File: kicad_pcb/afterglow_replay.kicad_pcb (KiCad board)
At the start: 2 copper layers, 49 x 111 mm, 106 parts, among them Q1 BC807, Q2 BC807, Q3 BC807, Q4 BC807, Q5 BC807, Q6 BC807, Q7 BC807, Q8 BC807, U1 ATmega328P-AU, U2 TLC5916IN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

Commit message: PCB v1.1
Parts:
- added USB PWR: USB_B_Micro, Connectors_USB:USB_Micro-B_Molex-105017-0001, B.Cu at (133.4, 46.4)
- C2: value 100nF -> 10uF; footprint Capacitors_SMD:C_0805_HandSoldering -> Capacitors_THT:CP_Radial_D5.0mm_P2.00mm
- C3, C4: value 16pF -> 18pF
- moved C2 65.0 mm to (128.3, 76.1)
- moved G*** 1.00 mm to (121.2, 53.5)
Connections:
- C2 pad 1: /RESET -> GND
- C2 pad 2: Net-(C2-Pad2) -> +3V3
- D12 pad 2: Net-(D12-Pad2) -> Net-(D11-Pad2)
- D13 pad 2: Net-(D12-Pad2) -> Net-(D11-Pad2)
- D14 pad 2: Net-(D12-Pad2) -> Net-(D11-Pad2)
- D15 pad 2: Net-(D12-Pad2) -> Net-(D11-Pad2)
- D16 pad 2: Net-(D12-Pad2) -> Net-(D11-Pad2)
- D17 pad 2: Net-(D12-Pad2) -> Net-(D11-Pad2)
- D18 pad 2: Net-(D12-Pad2) -> Net-(D11-Pad2)
- D22 pad 2: Net-(D22-Pad2) -> Net-(D21-Pad2)
- D23 pad 2: Net-(D22-Pad2) -> Net-(D21-Pad2)
- D24 pad 2: Net-(D22-Pad2) -> Net-(D21-Pad2)
- D25 pad 2: Net-(D22-Pad2) -> Net-(D21-Pad2)
- D26 pad 2: Net-(D22-Pad2) -> Net-(D21-Pad2)
- D27 pad 2: Net-(D22-Pad2) -> Net-(D21-Pad2)
- D28 pad 2: Net-(D22-Pad2) -> Net-(D21-Pad2)
- D32 pad 2: Net-(D32-Pad2) -> Net-(D31-Pad2)
- D33 pad 2: Net-(D32-Pad2) -> Net-(D31-Pad2)
- D34 pad 2: Net-(D32-Pad2) -> Net-(D31-Pad2)
- D35 pad 2: Net-(D32-Pad2) -> Net-(D31-Pad2)
- D36 pad 2: Net-(D32-Pad2) -> Net-(D31-Pad2)
- D37 pad 2: Net-(D32-Pad2) -> Net-(D31-Pad2)
- D38 pad 2: Net-(D32-Pad2) -> Net-(D31-Pad2)
- D42 pad 2: Net-(D42-Pad2) -> Net-(D41-Pad2)
- D43 pad 2: Net-(D42-Pad2) -> Net-(D41-Pad2)
- D44 pad 2: Net-(D42-Pad2) -> Net-(D41-Pad2)
- D45 pad 2: Net-(D42-Pad2) -> Net-(D41-Pad2)
- D46 pad 2: Net-(D42-Pad2) -> Net-(D41-Pad2)
- D47 pad 2: Net-(D42-Pad2) -> Net-(D41-Pad2)
- D48 pad 2: Net-(D42-Pad2) -> Net-(D41-Pad2)
- D52 pad 2: Net-(D52-Pad2) -> Net-(D51-Pad2)
- D53 pad 2: Net-(D52-Pad2) -> Net-(D51-Pad2)
- D54 pad 2: Net-(D52-Pad2) -> Net-(D51-Pad2)
- D55 pad 2: Net-(D52-Pad2) -> Net-(D51-Pad2)
- D56 pad 2: Net-(D52-Pad2) -> Net-(D51-Pad2)
- D57 pad 2: Net-(D52-Pad2) -> Net-(D51-Pad2)
- D58 pad 2: Net-(D52-Pad2) -> Net-(D51-Pad2)
- D62 pad 2: Net-(D62-Pad2) -> Net-(D61-Pad2)
- D63 pad 2: Net-(D62-Pad2) -> Net-(D61-Pad2)
- D64 pad 2: Net-(D62-Pad2) -> Net-(D61-Pad2)
- D65 pad 2: Net-(D62-Pad2) -> Net-(D61-Pad2)
- D66 pad 2: Net-(D62-Pad2) -> Net-(D61-Pad2)
- D67 pad 2: Net-(D62-Pad2) -> Net-(D61-Pad2)
- D68 pad 2: Net-(D62-Pad2) -> Net-(D61-Pad2)
- D72 pad 2: Net-(D72-Pad2) -> Net-(D71-Pad2)
- D73 pad 2: Net-(D72-Pad2) -> Net-(D71-Pad2)
- D74 pad 2: Net-(D72-Pad2) -> Net-(D71-Pad2)
- D75 pad 2: Net-(D72-Pad2) -> Net-(D71-Pad2)
- D76 pad 2: Net-(D72-Pad2) -> Net-(D71-Pad2)
- D77 pad 2: Net-(D72-Pad2) -> Net-(D71-Pad2)
- D78 pad 2: Net-(D72-Pad2) -> Net-(D71-Pad2)
- D82 pad 2: Net-(D82-Pad2) -> Net-(D81-Pad2)
- D83 pad 2: Net-(D82-Pad2) -> Net-(D81-Pad2)
- D84 pad 2: Net-(D82-Pad2) -> Net-(D81-Pad2)
- D85 pad 2: Net-(D82-Pad2) -> Net-(D81-Pad2)
- D86 pad 2: Net-(D82-Pad2) -> Net-(D81-Pad2)
- D87 pad 2: Net-(D82-Pad2) -> Net-(D81-Pad2)
- D88 pad 2: Net-(D82-Pad2) -> Net-(D81-Pad2)
- ISP pad 5: Net-(C2-Pad2) -> /RESET
- R12 pad 1: /SCK -> Net-(R12-Pad1)
- U1 pad 13: /SCK -> Net-(R12-Pad1)
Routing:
- net Net-(D81-Pad2): track 30.0 -> 161.5 mm, vias 1 -> 4
- net Net-(D82-Pad2): track 130.4 -> 0.00 mm, vias 3 -> 0
- net Net-(D21-Pad2): track 58.0 -> 149.7 mm
- net Net-(D22-Pad2): track 91.2 -> 0.00 mm
- net Net-(D31-Pad2): track 45.2 -> 119.6 mm, vias 1 -> 4
- net Net-(D32-Pad2): track 72.5 -> 0.00 mm, vias 2 -> 0
- net Net-(D51-Pad2): track 22.2 -> 90.0 mm, vias 1 -> 3
- net Net-(D52-Pad2): track 66.5 -> 0.00 mm, vias 2 -> 0
- net Net-(R12-Pad1): track 0.00 -> 52.4 mm, vias 0 -> 4
- net Net-(D61-Pad2): track 15.7 -> 63.7 mm
- net Net-(D62-Pad2): track 41.2 -> 0.00 mm
- net Net-(D71-Pad2): track 57.8 -> 97.7 mm
- net Net-(D72-Pad2): track 37.4 -> 0.00 mm
- net Net-(D11-Pad2): track 30.9 -> 64.1 mm, vias 1 -> 2
- net Net-(D41-Pad2): track 40.9 -> 70.8 mm
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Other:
- board text added: "REPLAY v1.1"
- board text removed: "REPLAY v1.0"

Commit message: PCB v1.2
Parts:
- added J5: Conn_01x02_Male, Pin_Headers:Pin_Header_Straight_1x02_Pitch2.54mm, B.Cu at (123.1, 45.9)
- added J6: Conn_01x02_Male, Pin_Headers:Pin_Header_Straight_1x02_Pitch2.54mm, B.Cu at (143.0, 45.9)
- C2: footprint Capacitors_THT:CP_Radial_D5.0mm_P2.00mm -> Capacitors_SMD:CP_Elec_4x5.3
- J4: renamed from USB PWR
- moved C2 1.03 mm to (127.4, 75.6)
- renumbered PWR to J1, SER to J2, ISP to J3, RST to SW1
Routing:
- net +3V3: track 361.8 -> 391.3 mm
- net GND: track 235.1 -> 247.5 mm
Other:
- board text added: "REPLAY v1.2"
- board text removed: "REPLAY v1.1"

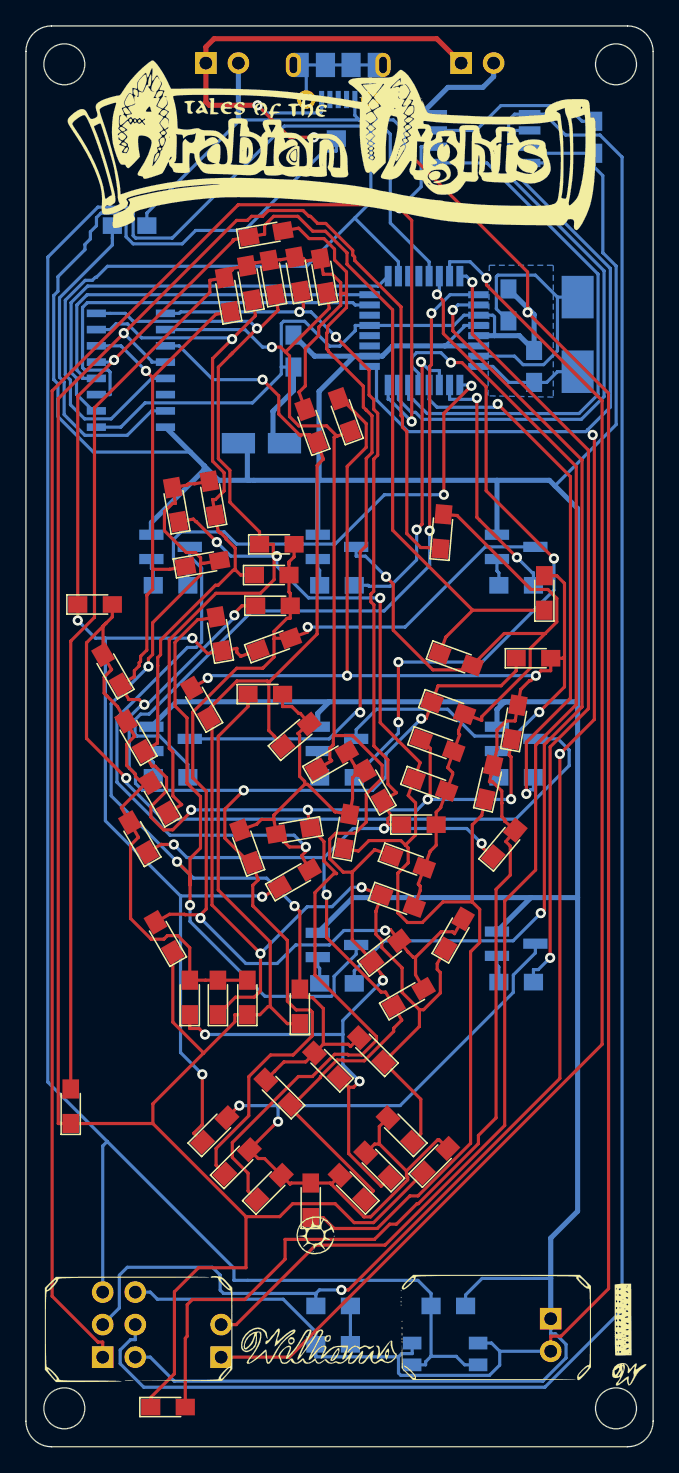
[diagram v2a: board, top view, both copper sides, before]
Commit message: PCB v1.2 slightly less wide
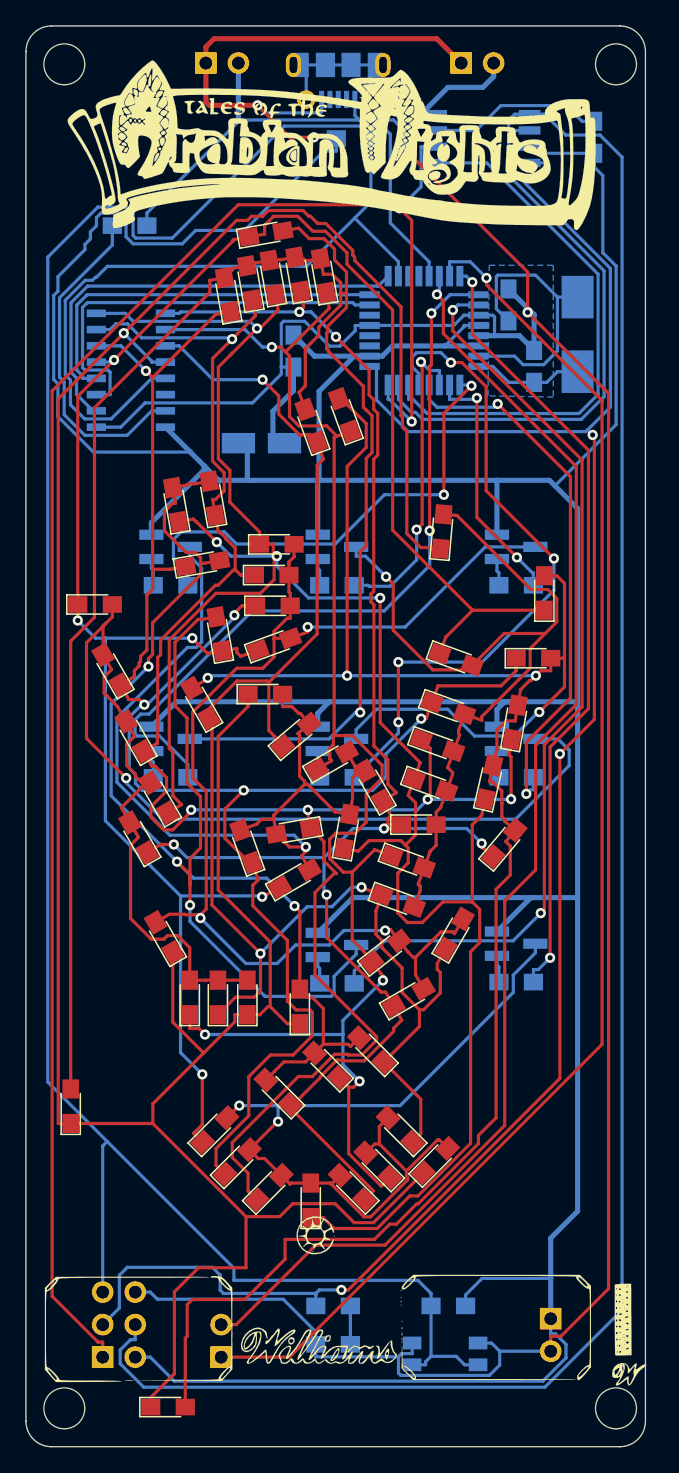
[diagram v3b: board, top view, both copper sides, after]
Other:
- board size 49 x 111 mm -> 48.4 x 111 mm
